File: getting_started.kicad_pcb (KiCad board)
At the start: 2 copper layers, 36.7 x 12.6 mm, 13 parts, among them J1 Prog connector, J2 Conn_01x03_Pin, U1 STM32F030F4Px, U2 SHT4x

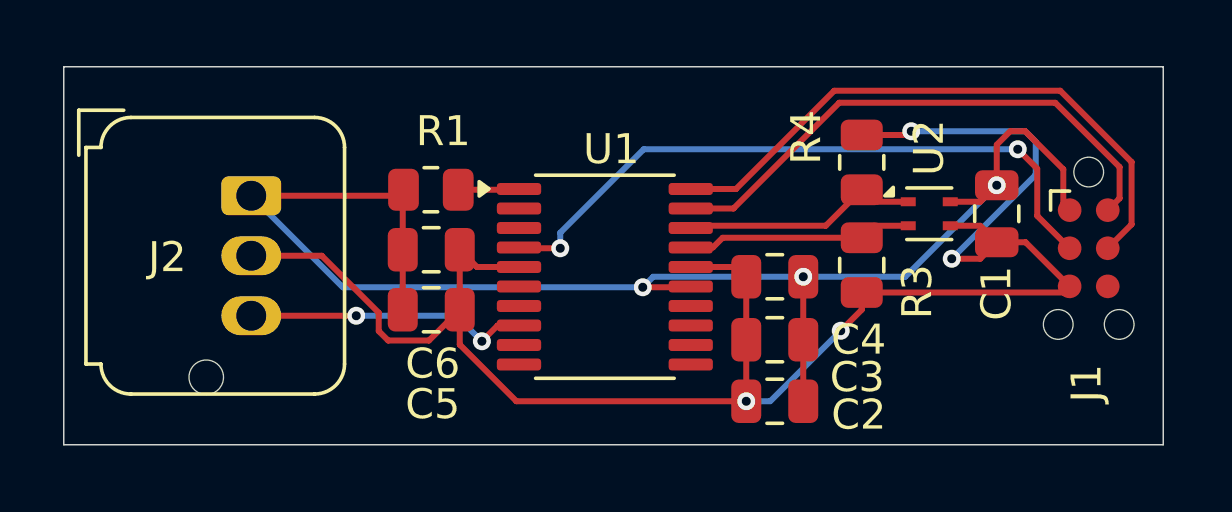
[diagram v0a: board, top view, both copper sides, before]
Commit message: Updated JST connector
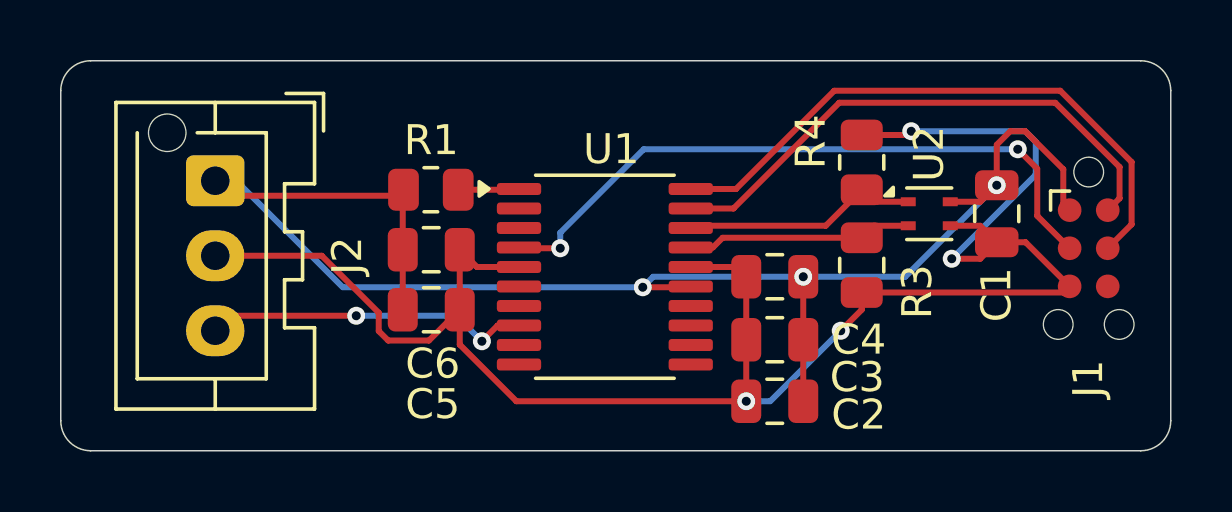
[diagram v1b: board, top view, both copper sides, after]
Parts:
- J2: footprint Connector_JST:JST_JWPF_B03B-JWPF-SK-R_1x03_P2.00mm_Vertical -> Connector_JST:JST_XA_B03B-XASK-1-A_1x03_P2.50mm_Vertical
- moved J2 1.30 mm to (103.3, 109.8), turned to -90 degrees
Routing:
- net GND: track 50.0 -> 52.8 mm
- net /IO: track 9.49 -> 10.9 mm
- net +3.3V: track 61.1 -> 62.3 mm
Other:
- board size 36.7 x 12.6 mm -> 37 x 13 mm

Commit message: Updated schematic and pcb
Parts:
- removed the C4 at (122.0, 113.0)
- J1: value Prog connector -> Conn_01x04_Pin; footprint Connector:Tag-Connect_TC2030-IDC-NL_2x03_P1.27mm_Vertical -> Connector_JST:JST_XA_B04B-XASK-1-A_1x04_P2.50mm_Vertical
- J2: value Conn_01x03_Pin -> Conn_ARM_JTAG_SWD_10; footprint Connector_JST:JST_XA_B03B-XASK-1-A_1x03_P2.50mm_Vertical -> Connector_PinHeader_1.27mm:PinHeader_2x05_P1.27mm_Vertical
- moved J1 18.0 mm to (115.8, 105.1), turned to 180 degrees
- moved R3 17.4 mm to (112.6, 121.5), turned to 180 degrees
- moved C2 16.5 mm to (107.8, 123.5), turned to 180 degrees
- moved C5 16.4 mm to (117.8, 122.5)
- moved U2 16.4 mm to (115.5, 122.5)
- moved R2 16.4 mm to (112.6, 123.5), turned to 180 degrees
- moved J2 15.7 mm to (117.2, 117.1), turned to 180 degrees
- moved C1 14.8 mm to (107.8, 121.5), turned to 180 degrees
- moved U1 8.30 mm to (108.8, 116.6), turned to -90 degrees
- moved C3 3.22 mm to (108.2, 111.8)
- moved C4 3.20 mm to (108.2, 109.8)
- moved R1 1.65 mm to (111.8, 111.1), turned to 90 degrees
- renumbered C3 to C1, C5 to C3, C6 to C4, C1 to C5, R3 to R2, R4 to R3
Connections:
- J1 pad 2: /SWDIO -> +3.3V
- J1 pad 3: /nReset -> /IO_TX
- J1 pad 4: /SWCLK -> /IO_RX
- J2 pad 1: GND -> +3.3V
- J2 pad 2: +3.3V -> /SWDIO
- J2 pad 3: /IO -> GND
- U1 pad 10: unconnected-(U1-PA4-Pad10) -> GND
- U1 pad 11: unconnected-(U1-PA5-Pad11) -> GND
- U1 pad 12: unconnected-(U1-PA6-Pad12) -> GND
- U1 pad 13: unconnected-(U1-PA7-Pad13) -> GND
- U1 pad 14: unconnected-(U1-PB1-Pad14) -> GND
- U1 pad 2: unconnected-(U1-PF0-Pad2) -> GND
- U1 pad 3: unconnected-(U1-PF1-Pad3) -> GND
- U1 pad 4: /nReset -> /nRESET
- U1 pad 6: unconnected-(U1-PA0-Pad6) -> GND
- U1 pad 7: unconnected-(U1-PA1-Pad7) -> GND
- U1 pad 8: /IO -> /IO_TX
- U1 pad 9: unconnected-(U1-PA3-Pad9) -> /IO_RX
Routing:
- net GND: track 52.8 -> 2.45 mm, vias 3 -> 6
- net /nReset: track 22.3 -> 0.00 mm, vias 2 -> 0
- net /SWCLK: track 20.2 -> 6.22 mm
- net /IO_TX: track 0.00 -> 13.0 mm, vias 0 -> 1
- net /IO_RX: track 0.00 -> 12.3 mm, vias 0 -> 1
- net /SWDIO: track 18.2 -> 6.98 mm
- net /IO: track 10.9 -> 0.00 mm, vias 2 -> 0
- net /nRESET: track 0.00 -> 8.05 mm
- net +3.3V: track 62.3 -> 58.9 mm, vias 4 -> 0
- net Net-(U1-PA9): track 7.55 -> 10.5 mm, vias 0 -> 2
- net Net-(U1-PA10): track 7.94 -> 8.36 mm, vias 0 -> 2
- added copper zone on B.Cu, net GND
- added copper zone on F.Cu, net GND
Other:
- board size 37 x 13 mm -> 16 x 25 mm

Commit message: Added power plane
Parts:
- moved C5 0.08 mm to (117.8, 122.5)
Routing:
- net +3.3V: track 58.9 -> 19.3 mm
- net GND: track 2.45 -> 2.52 mm, vias 6 -> 4
- added copper zone on F.Cu, net +3.3V
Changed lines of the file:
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@@
 		)
 		(fp_text user "${REFERENCE}"
-			(at 0 0 90)
+			(at 0 0 180)
 			(layer "F.Fab")
 			(effects
@@
 	(footprint "Capacitor_SMD:C_0805_2012Metric"
 		(layer "F.Cu")
-		(at 117.75 122.45 90)
+		(at 117.825 122.45 90)
 		(descr "Capacitor SMD 0805 (2012 Metric), square (rectangular) end terminal, IPC-7351 nominal, (Body size source: IPC-SM-782 page 76, https://www.pcb-3d.com/wordpress/wp-content/uploads/ipc-sm-782a_amendment_1_and_2.pdf, https://docs.google.com/spreadsheets/d/1BsfQQcO9C6DZCsRaXUlFlo91Tg2WpOkGARC1WS5S8t0/edit?usp=sharing), generated with kicad-footprint-generator")
 		(tags "capacitor")
@@
 		)
 		(fp_text user "${REFERENCE}"
-			(at 0 0 90)
+			(at 0 0 180)
 			(layer "F.Fab")
 			(effects
@@
 		)
 		(fp_text user "${REFERENCE}"
-			(at 0 0 90)
+			(at 0 0 180)
 			(layer "F.Fab")
 			(effects
@@
 		)
 		(fp_text user "${REFERENCE}"
-			(at 0 0 90)
+			(at 0 0 180)
 			(layer "F.Fab")
 			(effects
@@
 		(fp_poly
 			(pts
-				(xy -3.86 -2.93) (xy -4.19 -2.69) (xy -4.19 -3.17)
+				(xy -2.85 -3.55) (xy -3.09 -3.88) (xy -2.61 -3.88)
 			)
 			(stroke
@@
 		)
 		(fp_text user "${REFERENCE}"
-			(at 0.0125 0 90)
+			(at 0.0125 0 180)
 			(layer "F.Fab")
 			(effects
@@
 		(tags "DFN NoLead")
 		(property "Reference" "U2"
-			(at -0.01 -1.625 180)
+			(at 0.125 -1.625 180)
 			(layer "F.SilkS")
 			(effects
@@
 		)
 		(fp_text user "${REFERENCE}"
-			(at 0.635 2.54 90)
+			(at 0.635 2.54 180)
 			(layer "F.Fab")
 			(effects
@@
 	)
 	(segment
+		(start 116.25 122.05)
+		(end 117.275 122.05)
+		(width 0.3)
+		(layer "F.Cu")
+		(net 3)
+	)
+	(segment
 		(start 108.5 119.475)
 		(end 108.525 119.5)
@@
 	)
 	(segment
-		(start 116.25 122.05)
-		(end 117.2 122.05)
-		(width 0.2)
-		(layer "F.Cu")
-		(net 3)
-	)
-	(segment
-		(start 117.2 122.05)
-		(end 117.75 121.5)
-		(width 0.2)
-		(layer "F.Cu")
-		(net 3)
-	)
-	(segment
 		(start 111.75 109.925)
 		(end 111.725 109.9)
 		(width 0.2)
+		(layer "F.Cu")
+		(net 3)
+	)
+	(segment
+		(start 117.275 122.05)
+		(end 117.825 121.5)
+		(width 0.3)
 		(layer "F.Cu")
 		(net 3)
@@
 	)
 	(via
-		(at 106.225 107.875)
+		(at 105.7 122.45)
 		(size 0.6)
 		(drill 0.3)
@@
 	)
 	(via
-		(at 106.225 107.875)
+		(at 106.1 110.8)
 		(size 0.6)
 		(drill 0.3)
@@
 		(net 3)
 	)
-	(via
-		(at 106.1 110.8)
-		(size 0.6)
-		(drill 0.3)
-		(layers "F.Cu" "B.Cu")
-		(free yes)
-		(net 3)
-	)
-	(via
-		(at 105.7 122.45)
-		(size 0.6)
-		(drill 0.3)
-		(layers "F.Cu" "B.Cu")
-		(free yes)
-		(net 3)
-	)
-	(segment
-		(start 108.75 123.475)
-		(end 109.825 124.55)
-		(width 0.3)
-		(layer "F.Cu")
-		(net 4)
-	)
 	(segment
 		(start 109.175 121.05)
@@
 	)
 	(segment
-		(start 114.225 124.125)
-		(end 117.025 124.125)
-		(width 0.3)
-		(layer "F.Cu")
-		(net 4)
-	)
-	(segment
 		(start 113.55 120.0221)
 		(end 115.6221 117.95)
 		(width 0.2)
-		(layer "F.Cu")
-		(net 4)
-	)
-	(segment
-		(start 107.674 124.551)
-		(end 105.451 124.551)
-		(width 0.3)
 		(layer "F.Cu")
 		(net 4)
@@
 	)
 	(segment
-		(start 110.075 108.3)
-		(end 109.15 109.225)
-		(width 0.5)
-		(layer "F.Cu")
-		(net 4)
-	)
-	(segment
 		(start 109.15 113.75)
 		(end 109.175 113.775)
 		(width 0.2)
-		(layer "F.Cu")
-		(net 4)
-	)
-	(segment
-		(start 107.19313 108.3)
-		(end 110.075 108.3)
-		(width 0.3)
-		(layer "F.Cu")
-		(net 4)
-	)
-	(segment
-		(start 117.025 124.125)
-		(end 117.75 123.4)
-		(width 0.3)
-		(layer "F.Cu")
-		(net 4)
-	)
-	(segment
-		(start 105.05 110.44313)
-		(end 107.19313 108.3)
-		(width 0.3)
-		(layer "F.Cu")
-		(net 4)
-	)
-	(segment
-		(start 105.05 124.15)
-		(end 105.05 110.44313)
-		(width 0.3)
-		(layer "F.Cu")
-		(net 4)
-	)
-	(segment
-		(start 105.451 124.551)
-		(end 105.05 124.15)
-		(width 0.3)
-		(layer "F.Cu")
-		(net 4)
-	)
-	(segment
-		(start 112.45 124.55)
-		(end 113.55 123.45)
-		(width 0.3)
 		(layer "F.Cu")
 		(net 4)
@@
 	)
 	(segment
-		(start 113.25 105.125)
-		(end 110.075 108.3)
-		(width 0.5)
-		(layer "F.Cu")
-		(net 4)
-	)
-	(segment
 		(start 109.175 119.5)
 		(end 109.175 121.05)
@@
 	)
 	(segment
-		(start 113.55 123.45)
-		(end 114.225 124.125)
-		(width 0.3)
-		(layer "F.Cu")
-		(net 4)
-	)
-	(segment
 		(start 116.325 117.95)
 		(end 117.15 117.125)
@@
 	)
 	(segment
-		(start 109.15 109.225)
-		(end 109.15 109.825)
+		(start 109.15 109.825)
+		(end 109.15 108.675)
 		(width 0.5)
-		(layer "F.Cu")
-		(net 4)
-	)
-	(segment
-		(start 108.75 123.475)
-		(end 107.674 124.551)
-		(width 0.3)
-		(layer "F.Cu")
-		(net 4)
-	)
-	(segment
-		(start 109.825 124.55)
-		(end 112.45 124.55)
-		(width 0.3)
 		(layer "F.Cu")
 		(net 4)
@@
 		(layer "B.Cu")
 		(net 12)
+	)
+	(zone
+		(net 4)
+		(net_name "+3.3V")
+		(layer "F.Cu")
+		(hatch edge 0.5)
+		(priority 1)
+		(connect_pads
+			(clearance 0.2)
+		)
+		(min_thickness 0.2)
+		(filled_areas_thickness no)
+		(fill yes
+			(thermal_gap 0.2)
+			(thermal_bridge_width 0.2)
+			(island_removal_mode 2)
+			(island_area_min 10)
+		)
+		(polygon
+			(pts
+				(xy 120.25 126.025) (xy 120.25 122.6) (xy 120.25 122.9) (xy 115.15 122.9) (xy 114.225 123.825) (xy 114.225 123.825)
+				(xy 114.225 123.375) (xy 108.1 123.375) (xy 108.1 124.225) (xy 108.1 124.225) (xy 105.425 124.225)
+				(xy 105.2 124) (xy 105.2 110.54313) (xy 106.84313 108.9) (xy 108.65 108.9) (xy 108.65 109.15) (xy 109.65 109.15)
+				(xy 109.65 109.1) (xy 112.775 105.975) (xy 114 105.975) (xy 114.3 105.675) (xy 114.3 99.225) (xy 102.575 99.225)
+				(xy 101.825 99.975) (xy 101.825 126.325) (xy 119.95 126.325)
+			)
+		)
 	)
 	(zone
@@
 		(filled_areas_thickness no)
 		(fill yes
-			(thermal_gap 0.3)
-			(thermal_bridge_width 0.3)
+			(thermal_gap 0.2)
+			(thermal_bridge_width 0.2)
 			(island_removal_mode 2)
-			(island_area_min 5)
+			(island_area_min 10)
 		)
 		(polygon
 			(pts
-				(xy 120.45 100) (xy 120.475 100.025) (xy 120.475 125.8) (xy 120.25 126.025) (xy 103.65 126.025)
-				(xy 103.575 125.95) (xy 103.575 100)
-			)
-		)
+				(xy 120.45 100) (xy 120.475 100.025) (xy 120.258984 121.7) (xy 120.248878 123.05) (xy 117.425 123.05)
+				(xy 117.425 121.5) (xy 116.5 121.5) (xy 115.625 121.5) (xy 111.4 125.95) (xy 103.575 125.95) (xy 103.575 100)
+			)
+		)

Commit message: Updated planes
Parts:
- moved C3 0.35 mm to (108.5, 111.8)
- moved C4 0.35 mm to (108.5, 109.8)
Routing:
- net /SWCLK: track 6.22 -> 6.98 mm
- net /IO_RX: track 12.3 -> 12.9 mm
- net GND: vias 4 -> 114
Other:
- board size 16 x 25 mm -> 17 x 26 mm

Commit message: Pass ERC and DRC
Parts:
- moved C5 0.09 mm to (117.7, 122.5)
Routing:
- net GND: track 2.52 -> 3.12 mm, vias 114 -> 62
- net (no net): vias 0 -> 1

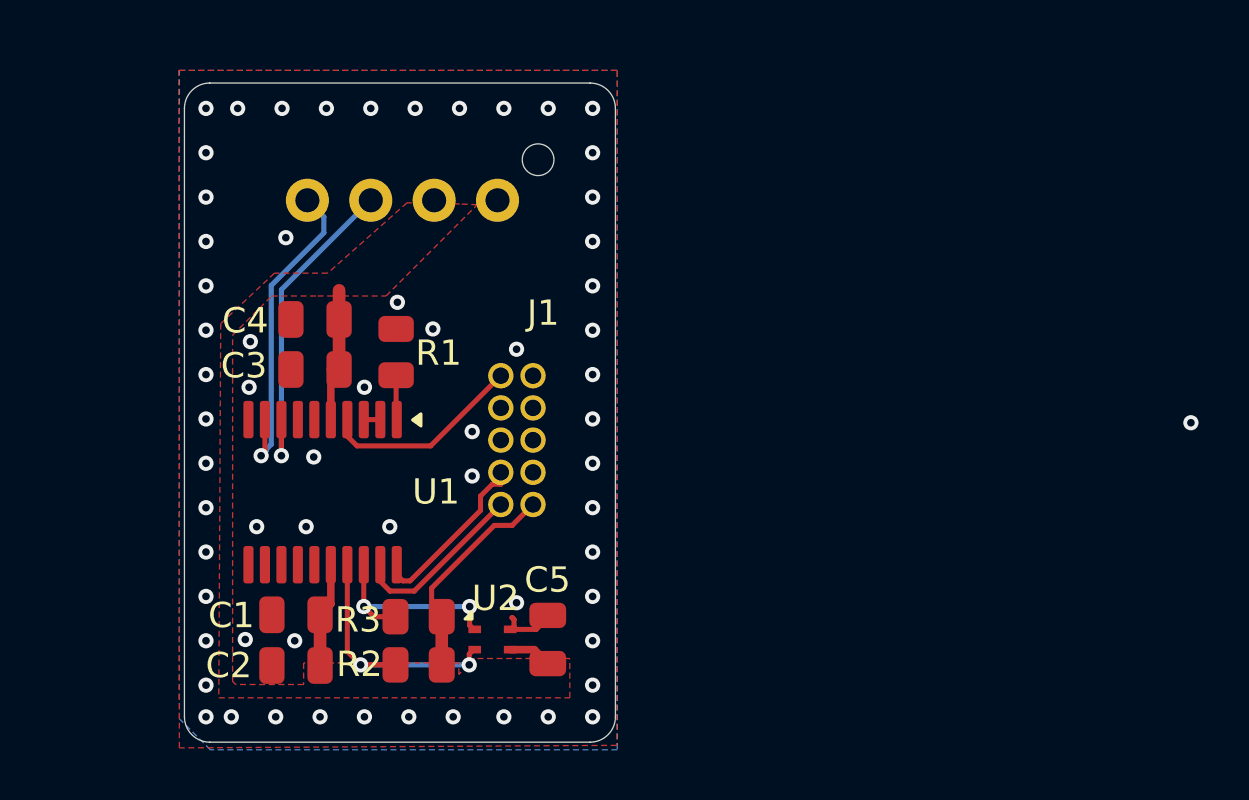
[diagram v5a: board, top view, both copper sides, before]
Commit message: Updated pcb layout
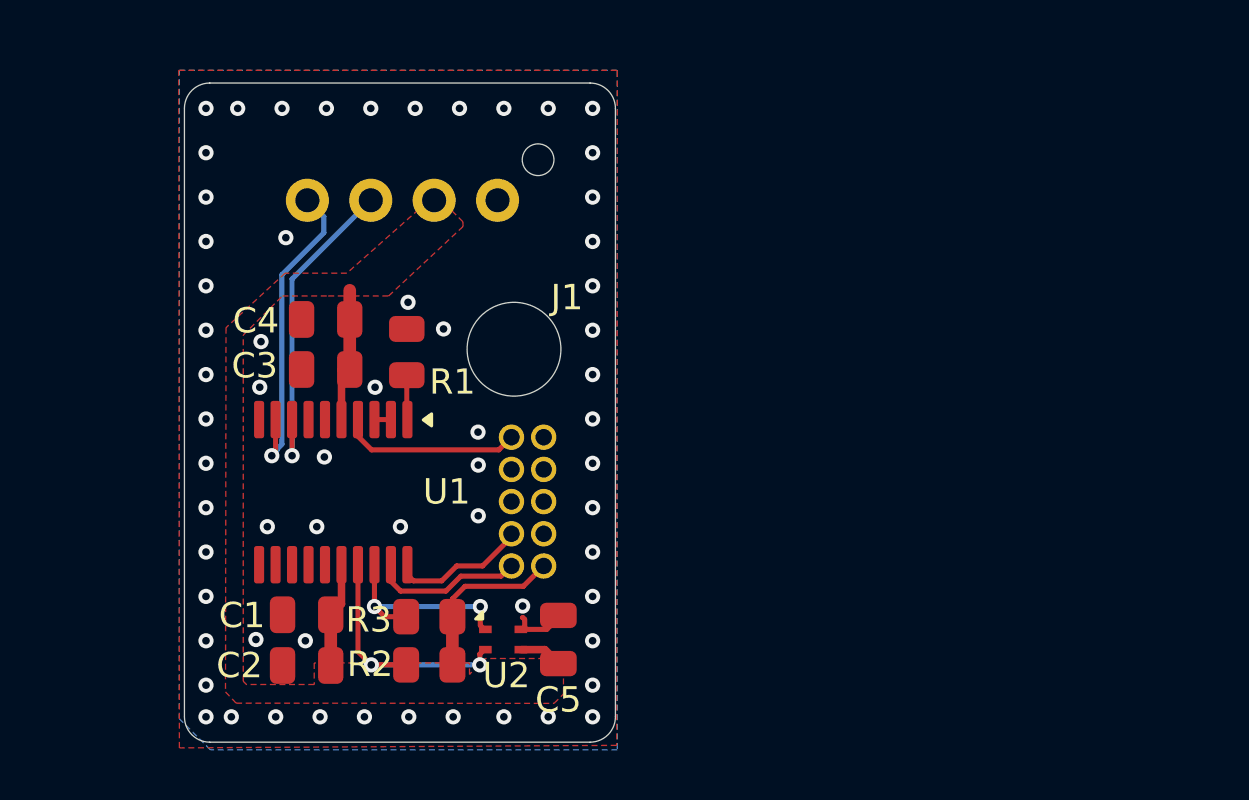
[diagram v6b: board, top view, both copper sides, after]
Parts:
- moved J2 2.46 mm to (117.6, 119.5)
- moved C1 0.42 mm to (108.2, 121.5)
- moved C2 0.42 mm to (108.2, 123.5)
- moved C3 0.42 mm to (109.0, 111.8)
- moved C4 0.42 mm to (109.0, 109.8)
- moved C5 0.42 mm to (118.2, 122.5)
- moved R1 0.42 mm to (112.2, 111.1)
- moved R2 0.42 mm to (113.1, 123.5)
- moved R3 0.42 mm to (113.1, 121.5)
- moved U1 0.42 mm to (109.3, 116.6)
- moved U2 0.42 mm to (116.0, 122.5)
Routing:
- net /SWCLK: track 6.98 -> 5.45 mm
- net +3.3V: track 19.6 -> 18.3 mm
- net /SWDIO: track 6.98 -> 5.98 mm
- net /nRESET: track 8.05 -> 7.18 mm
- net (no net): vias 1 -> 0
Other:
- outline, holes or cut-outs redrawn
- board text added: "Temperature/humidity sensor Richard I."
